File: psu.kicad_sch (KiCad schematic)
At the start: 23 parts, among them J2 13.8V, U5 TP6841, U6 TP6841

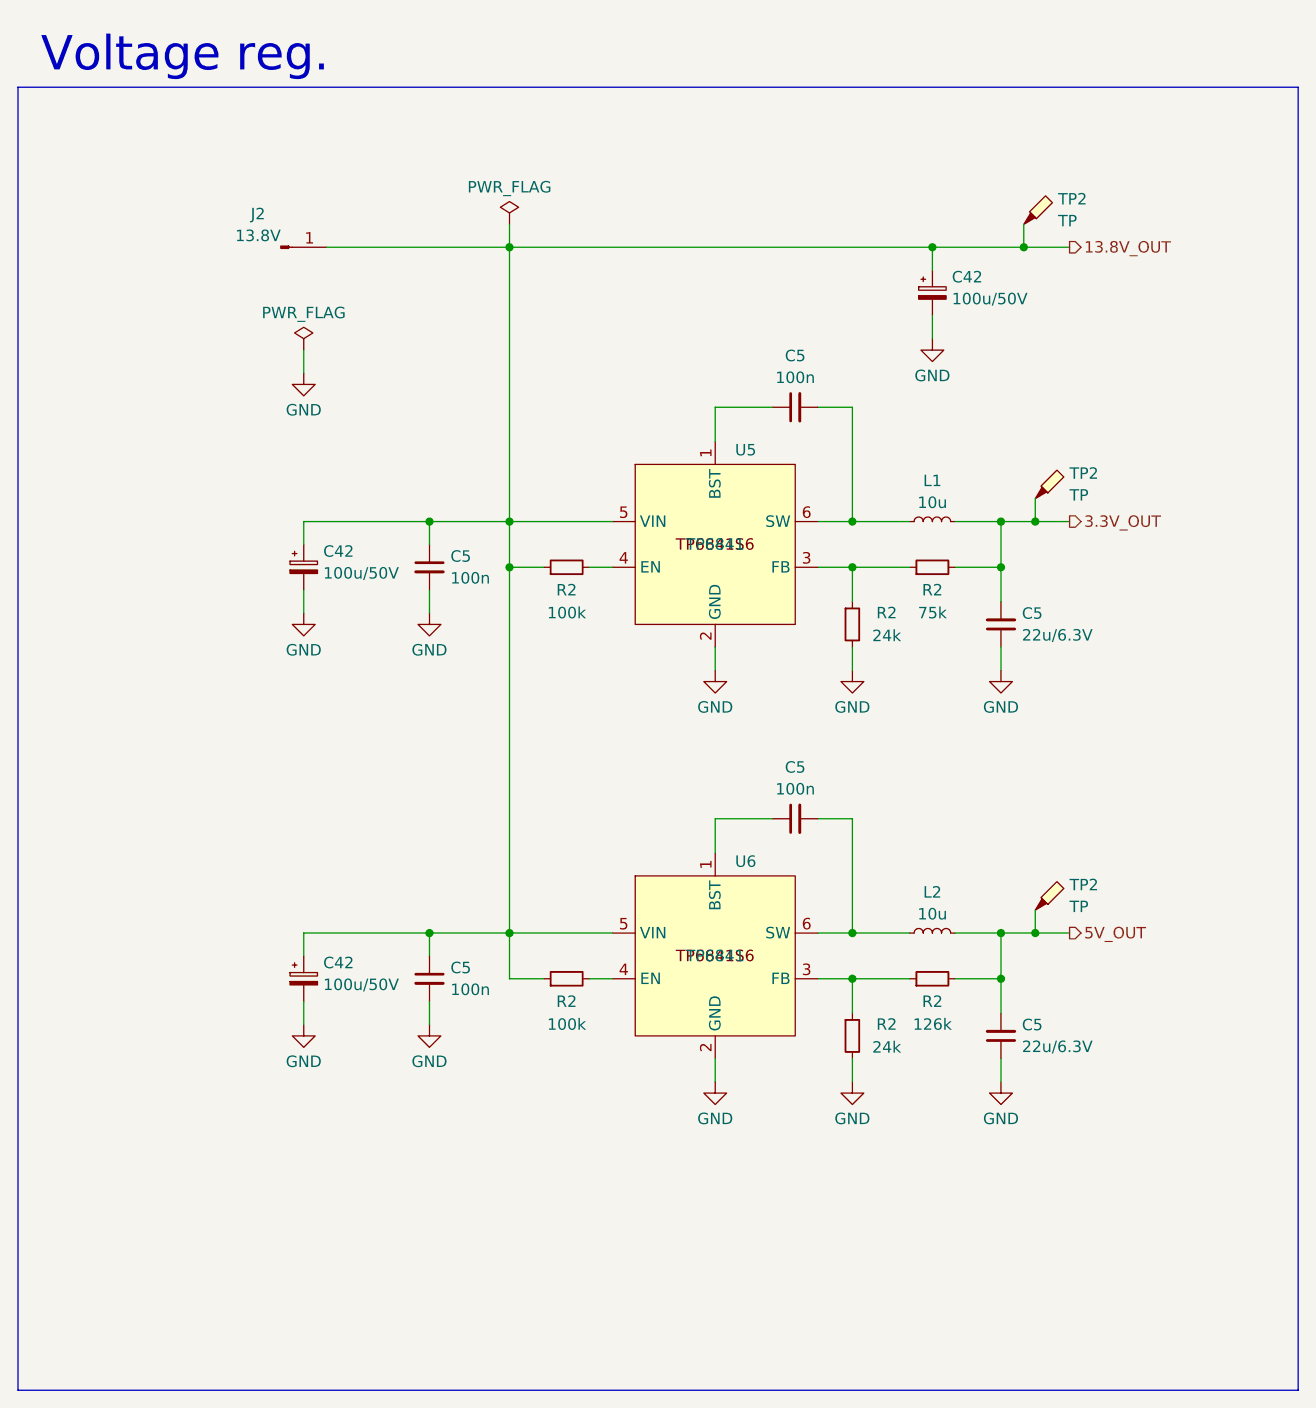
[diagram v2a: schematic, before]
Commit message: WIP rev B
- added bleed resistors
- power supply now uses linear regulators
- routed RX_SAMP_CLK
- added some decoupling at RF_PA_VDD
- added some GND vias here and there
- updated BOM
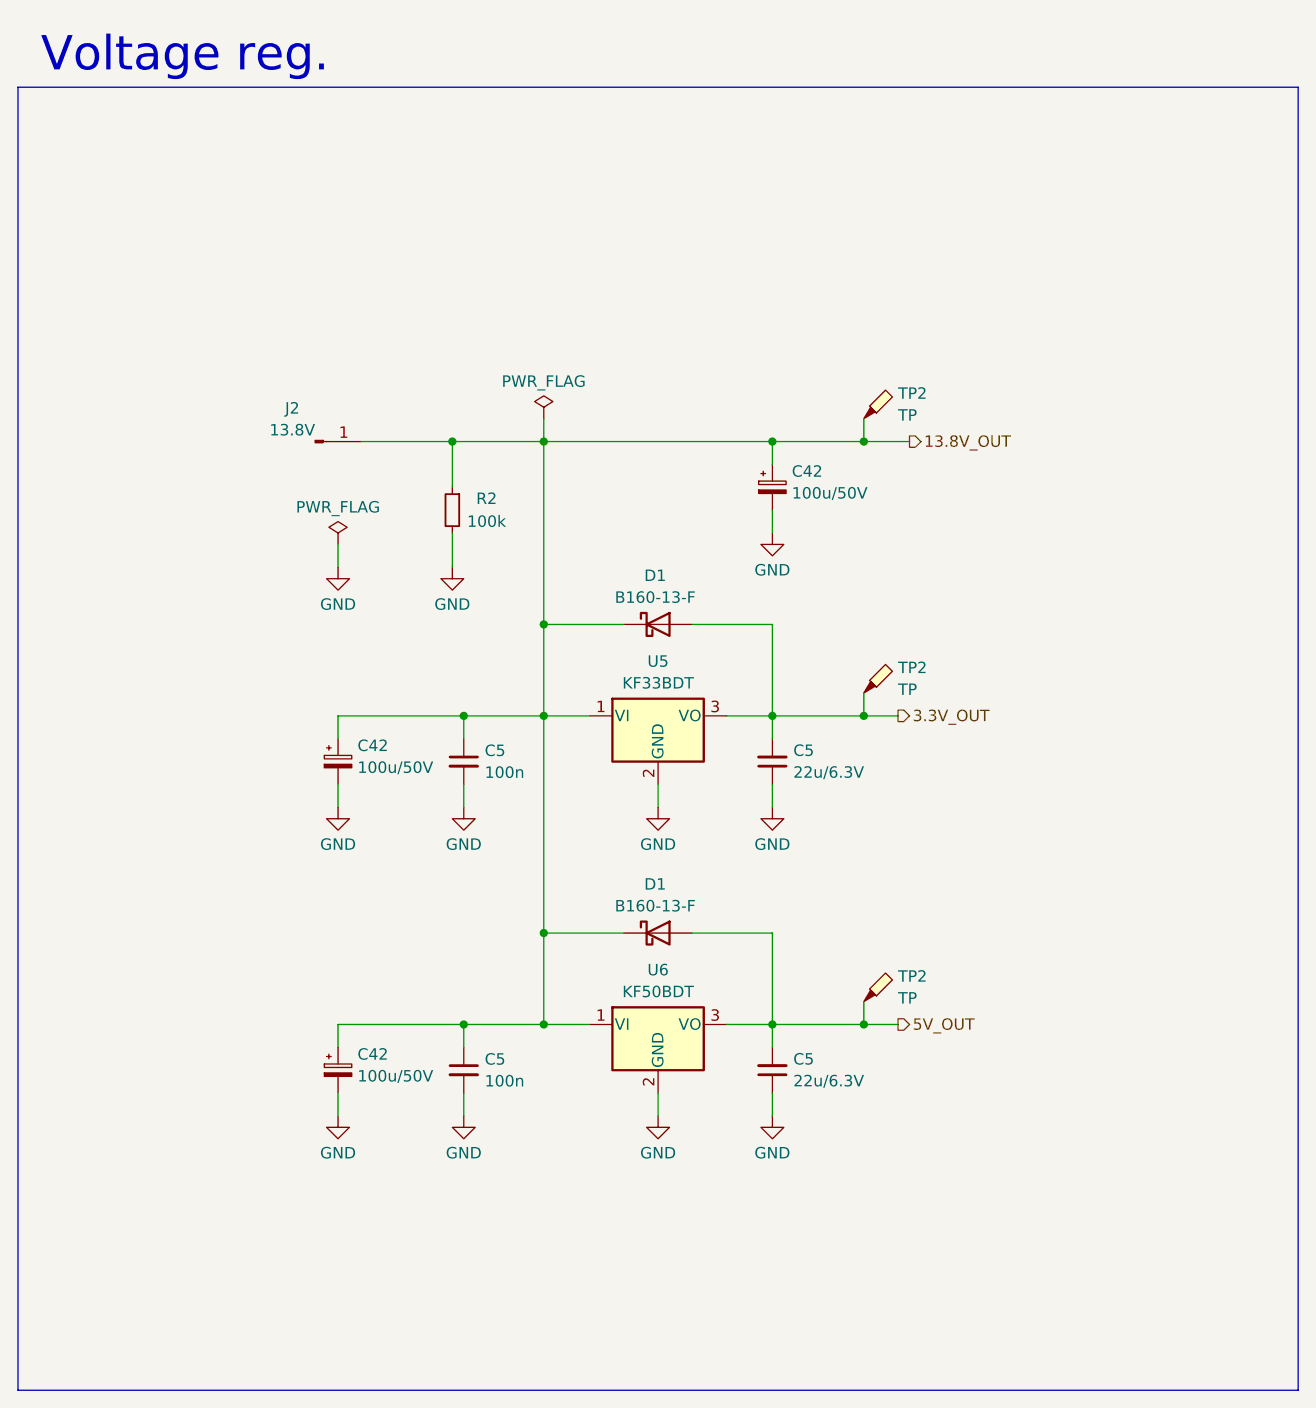
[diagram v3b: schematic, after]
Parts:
- removed C5 (x2): 100n, Capacitor_SMD:C_0603_1608Metric, symbol Device:C_Small
- removed L1, L2: 10u, Inductor_SMD:L_Vishay_IHLP-2525, symbol Device:L_Small
- removed R2: 126k, Resistor_SMD:R_0603_1608Metric, symbol Device:R_Small
- removed R2 (x2): 100k, Resistor_SMD:R_0603_1608Metric, symbol Device:R_Small
- removed R2: 75k, Resistor_SMD:R_0603_1608Metric, symbol Device:R_Small
- removed R2 (x2): 24k, Resistor_SMD:R_0603_1608Metric, symbol Device:R_Small
- removed U5, U6: TP6841, Package_TO_SOT_SMD:SOT-23-6, symbol Parts:TP6841S6-A
- added D1 (x2): B160-13-F, Diode_SMD:D_SMA, symbol Device:D_Schottky
- added R2: 100k, Resistor_SMD:R_0603_1608Metric, symbol Device:R_Small
- added U5: KF33BDT, Package_TO_SOT_SMD:TO-252-2, symbol Regulator_Linear:KF33BDT
- added U6: KF50BDT, Package_TO_SOT_SMD:TO-252-2, symbol Regulator_Linear:KF50BDT
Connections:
- net 13.8V_OUT: now also D1.1 (K), D1.1 (K), R2.1, U5.1 (VI), U6.1 (VI)
- net 3.3V_OUT: now also D1.2 (A), U5.3 (VO)
- net 5V_OUT: now also D1.2 (A), U6.3 (VO)
- net GND: now also R2.2, U5.2 (GND), U6.2 (GND)
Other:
- moved on the sheet: C42, C5, J2, TP2

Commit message: WIP rev C
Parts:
- renumbered C42 to C26, C42 to C27, C5 to C28, C5 to C29, C42 to C30, C5 to C31, C5 to C32, D1 to D6, D1 to D7, R2 to R23, TP2 to TP11, TP2 to TP12, TP2 to TP13
